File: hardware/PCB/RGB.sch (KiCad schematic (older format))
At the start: 24 parts, among them U1 IS31FL3733-QF, U2 IS31FL3733-QF

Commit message: making progress
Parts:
- U1, U2: value IS31FL3733-QF -> IS31FL3733-QFLS4-TR
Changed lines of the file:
@@
 P 7100 3600
 F 0 "U2" H 7100 1911 50  0000 C CNN
-F 1 "IS31FL3733-QF" H 7100 1820 50  0000 C CNN
+F 1 "IS31FL3733-QFLS4-TR" H 7100 1820 50  0000 C CNN
 F 2 "KiCad:QFN-48-1EP_6x6mm_P0.4mm_EP4.2x4.2mm_ThermalVias" H 7100 3600 50  0001 C CNN
 F 3 "http://www.issi.com/WW/pdf/IS31FL3733.pdf" H 7100 3600 50  0001 C CNN
@@
 P 4150 3600
 F 0 "U1" H 4150 1911 50  0000 C CNN
-F 1 "IS31FL3733-QF" H 4150 1820 50  0000 C CNN
+F 1 "IS31FL3733-QFLS4-TR" H 4150 1820 50  0000 C CNN
 F 2 "KiCad:QFN-48-1EP_6x6mm_P0.4mm_EP4.2x4.2mm_ThermalVias" H 4150 3600 50  0001 C CNN
 F 3 "http://www.issi.com/WW/pdf/IS31FL3733.pdf" H 4150 3600 50  0001 C CNN

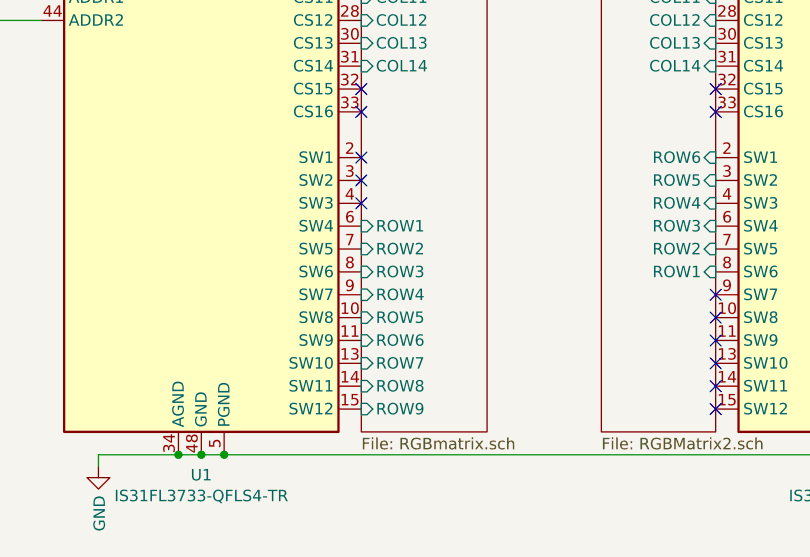
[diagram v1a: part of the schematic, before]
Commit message: Wiring now have no errors and uses less vias
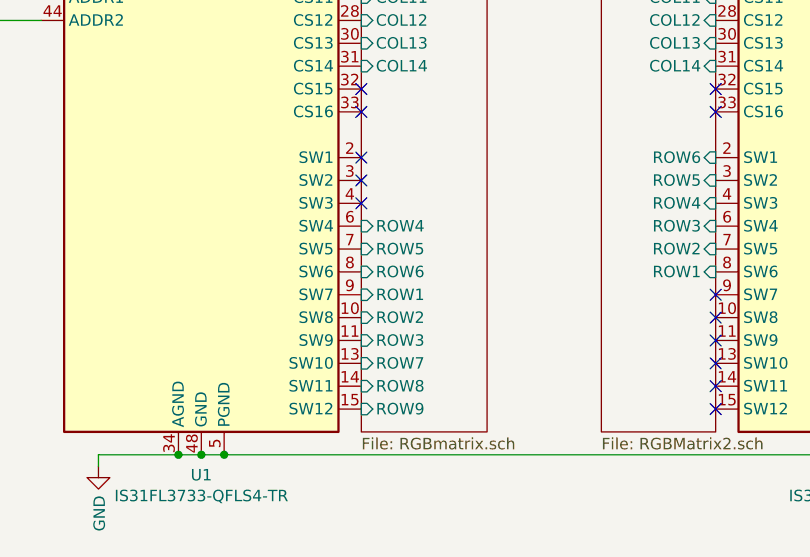
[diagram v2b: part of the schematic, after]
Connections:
- net RGBmatrix/ROW1: now also U1.9 (SW7); no longer U1.6 (SW4)
- net RGBmatrix/ROW2: now also U1.10 (SW8); no longer U1.7 (SW5)
- net RGBmatrix/ROW3: now also U1.11 (SW9); no longer U1.8 (SW6)
- net RGBmatrix/ROW4: now also U1.6 (SW4); no longer U1.9 (SW7)
- net RGBmatrix/ROW5: now also U1.7 (SW5); no longer U1.10 (SW8)
- net RGBmatrix/ROW6: now also U1.8 (SW6); no longer U1.11 (SW9)
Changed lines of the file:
@@
 F14 "COL13" I L 4850 3400 50
 F15 "COL14" I L 4850 3500 50
-F16 "ROW1" I L 4850 4200 50
-F17 "ROW2" I L 4850 4300 50
-F18 "ROW3" I L 4850 4400 50
-F19 "ROW4" I L 4850 4500 50
-F20 "ROW5" I L 4850 4600 50
-F21 "ROW6" I L 4850 4700 50
+F16 "ROW1" I L 4850 4500 50
+F17 "ROW2" I L 4850 4600 50
+F18 "ROW3" I L 4850 4700 50
+F19 "ROW4" I L 4850 4200 50
+F20 "ROW5" I L 4850 4300 50
+F21 "ROW6" I L 4850 4400 50
 F22 "ROW7" I L 4850 4800 50
 F23 "ROW8" I L 4850 4900 50

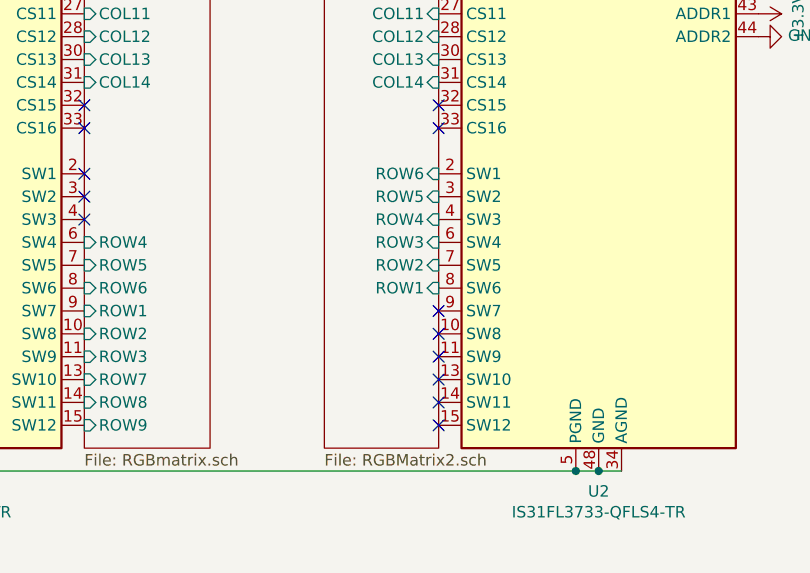
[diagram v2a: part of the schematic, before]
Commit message: minor changes to the LED controller PCB layout, make it much better
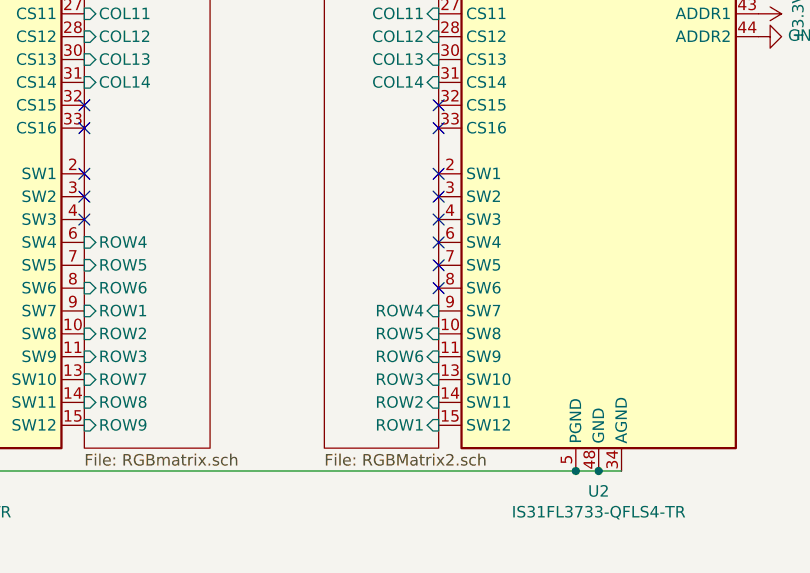
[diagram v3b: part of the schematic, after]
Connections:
- net RGBmatrix2/ROW1: now also U2.15 (SW12); no longer U2.8 (SW6)
- net RGBmatrix2/ROW2: now also U2.14 (SW11); no longer U2.7 (SW5)
- net RGBmatrix2/ROW3: now also U2.13 (SW10); no longer U2.6 (SW4)
- net RGBmatrix2/ROW4: now also U2.9 (SW7); no longer U2.4 (SW3)
- net RGBmatrix2/ROW5: now also U2.10 (SW8); no longer U2.3 (SW2)
- net RGBmatrix2/ROW6: now also U2.11 (SW9); no longer U2.2 (SW1)
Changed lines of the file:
@@
 Wire Wire Line
 	4250 5200 7000 5200
-NoConn ~ 6400 5000
-NoConn ~ 6400 4900
-NoConn ~ 6400 4800
-NoConn ~ 6400 4700
-NoConn ~ 6400 4600
-NoConn ~ 6400 4500
 NoConn ~ 6400 3700
 NoConn ~ 4850 3700
-$Sheet
-S 5900 2100 500  3000
-U 5E12F961
-F0 "RGBmatrix2" 50
-F1 "RGBMatrix2.sch" 50
-F2 "COL1" I R 6400 2200 50
-F3 "COL2" I R 6400 2300 50
-F4 "COL3" I R 6400 2400 50
-F5 "COL4" I R 6400 2500 50
-F6 "COL5" I R 6400 2600 50
-F7 "COL6" I R 6400 2700 50
-F8 "COL7" I R 6400 2800 50
-F9 "COL8" I R 6400 2900 50
-F10 "COL9" I R 6400 3000 50
-F11 "COL10" I R 6400 3100 50
-F12 "COL11" I R 6400 3200 50
-F13 "COL12" I R 6400 3300 50
-F14 "COL13" I R 6400 3400 50
-F15 "COL14" I R 6400 3500 50
-F16 "ROW1" I R 6400 4400 50
-F17 "ROW2" I R 6400 4300 50
-F18 "ROW3" I R 6400 4200 50
-F19 "ROW4" I R 6400 4100 50
-F20 "ROW5" I R 6400 4000 50
-F21 "ROW6" I R 6400 3900 50
-$EndSheet
 Wire Wire Line
 	3250 2100 3300 2100
@@
 NoConn ~ 4850 4000
 NoConn ~ 4850 3900
+NoConn ~ 6400 3900
+NoConn ~ 6400 4000
+NoConn ~ 6400 4100
+NoConn ~ 6400 4200
+NoConn ~ 6400 4300
+NoConn ~ 6400 4400
+$Sheet
+S 5900 2100 500  3000
+U 5E12F961
+F0 "RGBmatrix2" 50
+F1 "RGBMatrix2.sch" 50
+F2 "COL1" I R 6400 2200 50
+F3 "COL2" I R 6400 2300 50
+F4 "COL3" I R 6400 2400 50
+F5 "COL4" I R 6400 2500 50
+F6 "COL5" I R 6400 2600 50
+F7 "COL6" I R 6400 2700 50
+F8 "COL7" I R 6400 2800 50
+F9 "COL8" I R 6400 2900 50
+F10 "COL9" I R 6400 3000 50
+F11 "COL10" I R 6400 3100 50
+F12 "COL11" I R 6400 3200 50
+F13 "COL12" I R 6400 3300 50
+F14 "COL13" I R 6400 3400 50
+F15 "COL14" I R 6400 3500 50
+F16 "ROW1" I R 6400 5000 50
+F17 "ROW2" I R 6400 4900 50
+F18 "ROW3" I R 6400 4800 50
+F19 "ROW4" I R 6400 4500 50
+F20 "ROW5" I R 6400 4600 50
+F21 "ROW6" I R 6400 4700 50
+$EndSheet
 $EndSCHEMATC

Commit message: Now it should be working just fine
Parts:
- C1, C10, C12, C14, C2, C4, C6, C8: Footprint Capacitor_SMD:C_0402_1005Metric -> (none); Value 470nF -> (none)
- C11, C13, C3, C5, C7, C9: Footprint Capacitor_SMD:C_0402_1005Metric -> (none); Value 100nf -> (none)
- R1, R8: Footprint Resistor_SMD:R_0402_1005Metric -> (none); Value 100k -> (none)
- R2, R3, R5, R6: Footprint Resistor_SMD:R_0402_1005Metric -> (none); Value 1k -> (none)
- R4, R7: Footprint Resistor_SMD:R_0402_1005Metric -> (none); Value 20k -> (none)
- U1, U2: Footprint Package_DFN_QFN:QFN-48-1EP_6x6mm_P0.4mm_EP4.2x4.2mm_Thermal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 -> (none); Value IS31FL7377 -> (none)
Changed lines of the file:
@@
 F 2 "Resistor_SMD:R_0402_1005Metric" V 8230 3100 50  0001 C CNN
 F 3 "~" H 8300 3100 50  0001 C CNN
-F 4 "20k" H 8300 3100 50  0001 C CNN "Value"
-F 5 "Resistor_SMD:R_0402_1005Metric" H 8300 3100 50  0001 C CNN "Footprint"
 	1    8300 3100
 	0    -1   -1   0
@@
 F 2 "Resistor_SMD:R_0402_1005Metric" V 8330 2800 50  0001 C CNN
 F 3 "~" H 8400 2800 50  0001 C CNN
-F 4 "100k" H 8400 2800 50  0001 C CNN "Value"
-F 5 "Resistor_SMD:R_0402_1005Metric" H 8400 2800 50  0001 C CNN "Footprint"
 	1    8400 2800
 	0    -1   1    0
@@
 F 2 "Capacitor_SMD:C_0402_1005Metric" H 8050 2000 50  0001 C CNN
 F 3 "~" H 8050 2000 50  0001 C CNN
-F 4 "Capacitor_SMD:C_0402_1005Metric" H 8050 2000 50  0001 C CNN "Footprint"
-F 5 "470nF" H 8050 2000 50  0001 C CNN "Value"
 	1    8050 2000
 	-1   0    0    -1
@@
 F 2 "Resistor_SMD:R_0402_1005Metric" V 7880 2350 50  0001 C CNN
 F 3 "~" H 7950 2350 50  0001 C CNN
-F 4 "1k" H 7950 2350 50  0001 C CNN "Value"
-F 5 "Resistor_SMD:R_0402_1005Metric" H 7950 2350 50  0001 C CNN "Footprint"
 	1    7950 2350
 	-1   0    0    -1
@@
 F 2 "Resistor_SMD:R_0402_1005Metric" V 8080 2250 50  0001 C CNN
 F 3 "~" H 8150 2250 50  0001 C CNN
-F 4 "1k" H 8150 2250 50  0001 C CNN "Value"
-F 5 "Resistor_SMD:R_0402_1005Metric" H 8150 2250 50  0001 C CNN "Footprint"
 	1    8150 2250
 	-1   0    0    -1
@@
 F 2 "Capacitor_SMD:C_0402_1005Metric" H 3250 2000 50  0001 C CNN
 F 3 "~" H 3250 2000 50  0001 C CNN
-F 4 "Capacitor_SMD:C_0402_1005Metric" H 3250 2000 50  0001 C CNN "Footprint"
-F 5 "470nF" H 3250 2000 50  0001 C CNN "Value"
 	1    3250 2000
 	1    0    0    -1
@@
 F 2 "Resistor_SMD:R_0402_1005Metric" V 3230 3100 50  0001 C CNN
 F 3 "~" H 3300 3100 50  0001 C CNN
-F 4 "20k" H 3300 3100 50  0001 C CNN "Value"
-F 5 "Resistor_SMD:R_0402_1005Metric" H 3300 3100 50  0001 C CNN "Footprint"
 	1    3300 3100
 	0    1    1    0
@@
 F 2 "Resistor_SMD:R_0402_1005Metric" V 3230 2350 50  0001 C CNN
 F 3 "~" H 3300 2350 50  0001 C CNN
-F 4 "1k" H 3300 2350 50  0001 C CNN "Value"
-F 5 "Resistor_SMD:R_0402_1005Metric" H 3300 2350 50  0001 C CNN "Footprint"
 	1    3300 2350
 	1    0    0    -1
@@
 F 2 "Resistor_SMD:R_0402_1005Metric" V 3030 2250 50  0001 C CNN
 F 3 "~" H 3100 2250 50  0001 C CNN
-F 4 "1k" H 3100 2250 50  0001 C CNN "Value"
-F 5 "Resistor_SMD:R_0402_1005Metric" H 3100 2250 50  0001 C CNN "Footprint"
 	1    3100 2250
 	1    0    0    -1
@@
 F 2 "Resistor_SMD:R_0402_1005Metric" V 2780 2800 50  0001 C CNN
 F 3 "~" H 2850 2800 50  0001 C CNN
-F 4 "100k" H 2850 2800 50  0001 C CNN "Value"
-F 5 "Resistor_SMD:R_0402_1005Metric" H 2850 2800 50  0001 C CNN "Footprint"
 	1    2850 2800
 	0    1    1    0
@@
 F 2 "KiCad:QFN-48-1EP_6x6mm_P0.4mm_EP4.2x4.2mm_ThermalVias" H 7100 3600 50  0001 C CNN
 F 3 "http://www.issi.com/WW/pdf/IS31FL3733.pdf" H 7100 3600 50  0001 C CNN
-F 4 "IS31FL7377" H 7100 3600 50  0001 C CNN "Value"
-F 5 "Package_DFN_QFN:QFN-48-1EP_6x6mm_P0.4mm_EP4.2x4.2mm_ThermalVias" H 7100 3600 50  0001 C CNN "Footprint"
 	1    7100 3600
 	-1   0    0    -1
@@
 F 2 "KiCad:QFN-48-1EP_6x6mm_P0.4mm_EP4.2x4.2mm_ThermalVias" H 4150 3600 50  0001 C CNN
 F 3 "http://www.issi.com/WW/pdf/IS31FL3733.pdf" H 4150 3600 50  0001 C CNN
-F 4 "IS31FL7377" H 4150 3600 50  0001 C CNN "Value"
-F 5 "Package_DFN_QFN:QFN-48-1EP_6x6mm_P0.4mm_EP4.2x4.2mm_ThermalVias" H 4150 3600 50  0001 C CNN "Footprint"
 	1    4150 3600
 	1    0    0    -1
@@
 F 2 "Capacitor_SMD:C_0402_1005Metric" H 7100 1900 50  0001 C CNN
 F 3 "~" H 7100 1900 50  0001 C CNN
-F 4 "Capacitor_SMD:C_0402_1005Metric" H 7100 1900 50  0001 C CNN "Footprint"
-F 5 "100nf" H 7100 1900 50  0001 C CNN "Value"
 	1    7100 1900
 	0    -1   -1   0
@@
 F 2 "Capacitor_SMD:C_0402_1005Metric" H 7100 1150 50  0001 C CNN
 F 3 "~" H 7100 1150 50  0001 C CNN
-F 4 "Capacitor_SMD:C_0402_1005Metric" H 7100 1150 50  0001 C CNN "Footprint"
-F 5 "470nF" H 7100 1150 50  0001 C CNN "Value"
 	1    7100 1150
 	0    -1   -1   0
@@
 F 2 "Capacitor_SMD:C_0402_1005Metric" H 6650 1900 50  0001 C CNN
 F 3 "~" H 6650 1900 50  0001 C CNN
-F 4 "Capacitor_SMD:C_0402_1005Metric" H 6650 1900 50  0001 C CNN "Footprint"
-F 5 "100nf" H 6650 1900 50  0001 C CNN "Value"
 	1    6650 1900
 	0    -1   -1   0
@@
 F 2 "Capacitor_SMD:C_0402_1005Metric" H 6650 1150 50  0001 C CNN
 F 3 "~" H 6650 1150 50  0001 C CNN
-F 4 "Capacitor_SMD:C_0402_1005Metric" H 6650 1150 50  0001 C CNN "Footprint"
-F 5 "470nF" H 6650 1150 50  0001 C CNN "Value"
 	1    6650 1150
 	0    -1   -1   0
@@
 F 2 "Capacitor_SMD:C_0402_1005Metric" H 7550 1900 50  0001 C CNN
 F 3 "~" H 7550 1900 50  0001 C CNN
-F 4 "Capacitor_SMD:C_0402_1005Metric" H 7550 1900 50  0001 C CNN "Footprint"
-F 5 "100nf" H 7550 1900 50  0001 C CNN "Value"
 	1    7550 1900
 	0    -1   -1   0
@@
 F 2 "Capacitor_SMD:C_0402_1005Metric" H 7550 1150 50  0001 C CNN
 F 3 "~" H 7550 1150 50  0001 C CNN
-F 4 "Capacitor_SMD:C_0402_1005Metric" H 7550 1150 50  0001 C CNN "Footprint"
-F 5 "470nF" H 7550 1150 50  0001 C CNN "Value"
 	1    7550 1150
 	0    -1   -1   0
@@
 F 2 "Capacitor_SMD:C_0402_1005Metric" H 4350 1900 50  0001 C CNN
 F 3 "~" H 4350 1900 50  0001 C CNN
-F 4 "Capacitor_SMD:C_0402_1005Metric" H 4350 1900 50  0001 C CNN "Footprint"
-F 5 "100nf" H 4350 1900 50  0001 C CNN "Value"
 	1    4350 1900
 	0    -1   -1   0
@@
 F 2 "Capacitor_SMD:C_0402_1005Metric" H 4350 1150 50  0001 C CNN
 F 3 "~" H 4350 1150 50  0001 C CNN
-F 4 "Capacitor_SMD:C_0402_1005Metric" H 4350 1150 50  0001 C CNN "Footprint"
-F 5 "470nF" H 4350 1150 50  0001 C CNN "Value"
 	1    4350 1150
 	0    -1   -1   0
@@
 F 2 "Capacitor_SMD:C_0402_1005Metric" H 3800 1900 50  0001 C CNN
 F 3 "~" H 3800 1900 50  0001 C CNN
-F 4 "Capacitor_SMD:C_0402_1005Metric" H 3800 1900 50  0001 C CNN "Footprint"
-F 5 "100nf" H 3800 1900 50  0001 C CNN "Value"
 	1    3800 1900
 	0    -1   -1   0
@@
 F 2 "Capacitor_SMD:C_0402_1005Metric" H 3800 1150 50  0001 C CNN
 F 3 "~" H 3800 1150 50  0001 C CNN
-F 4 "Capacitor_SMD:C_0402_1005Metric" H 3800 1150 50  0001 C CNN "Footprint"
-F 5 "470nF" H 3800 1150 50  0001 C CNN "Value"
 	1    3800 1150
 	0    -1   -1   0
@@
 F 2 "Capacitor_SMD:C_0402_1005Metric" H 4700 1900 50  0001 C CNN
 F 3 "~" H 4700 1900 50  0001 C CNN
-F 4 "Capacitor_SMD:C_0402_1005Metric" H 4700 1900 50  0001 C CNN "Footprint"
-F 5 "100nf" H 4700 1900 50  0001 C CNN "Value"
 	1    4700 1900
 	0    -1   -1   0
@@
 F 2 "Capacitor_SMD:C_0402_1005Metric" H 4700 1150 50  0001 C CNN
 F 3 "~" H 4700 1150 50  0001 C CNN
-F 4 "Capacitor_SMD:C_0402_1005Metric" H 4700 1150 50  0001 C CNN "Footprint"
-F 5 "470nF" H 4700 1150 50  0001 C CNN "Value"
 	1    4700 1150
 	0    -1   -1   0

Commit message: add in part number so I could use it for the bom
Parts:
- U1, U2: Part Number (none) -> IS31FL3733-QFLS4-TR
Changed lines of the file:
@@
 F 2 "KiCad:QFN-48-1EP_6x6mm_P0.4mm_EP4.2x4.2mm_ThermalVias" H 7100 3600 50  0001 C CNN
 F 3 "http://www.issi.com/WW/pdf/IS31FL3733.pdf" H 7100 3600 50  0001 C CNN
+F 4 "IS31FL3733-QFLS4-TR" H 7100 3600 50  0001 C CNN "Part Number"
 	1    7100 3600
 	-1   0    0    -1
@@
 F 2 "KiCad:QFN-48-1EP_6x6mm_P0.4mm_EP4.2x4.2mm_ThermalVias" H 4150 3600 50  0001 C CNN
 F 3 "http://www.issi.com/WW/pdf/IS31FL3733.pdf" H 4150 3600 50  0001 C CNN
+F 4 "IS31FL3733-QFLS4-TR" H 4150 3600 50  0001 C CNN "Part Number"
 	1    4150 3600
 	1    0    0    -1
